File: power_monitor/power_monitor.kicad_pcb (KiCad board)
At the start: 2 copper layers, 60 x 62 mm, 22 parts, among them J1 230V AC Input, J2 230V AC Output, J3 RFID, J4 OLED, J5 WS2812, K1 G2RL-2A-DC5, Q1 FDN339AN, U1 Wemos-D1-mini, U2 ACS723xMATR-10AB

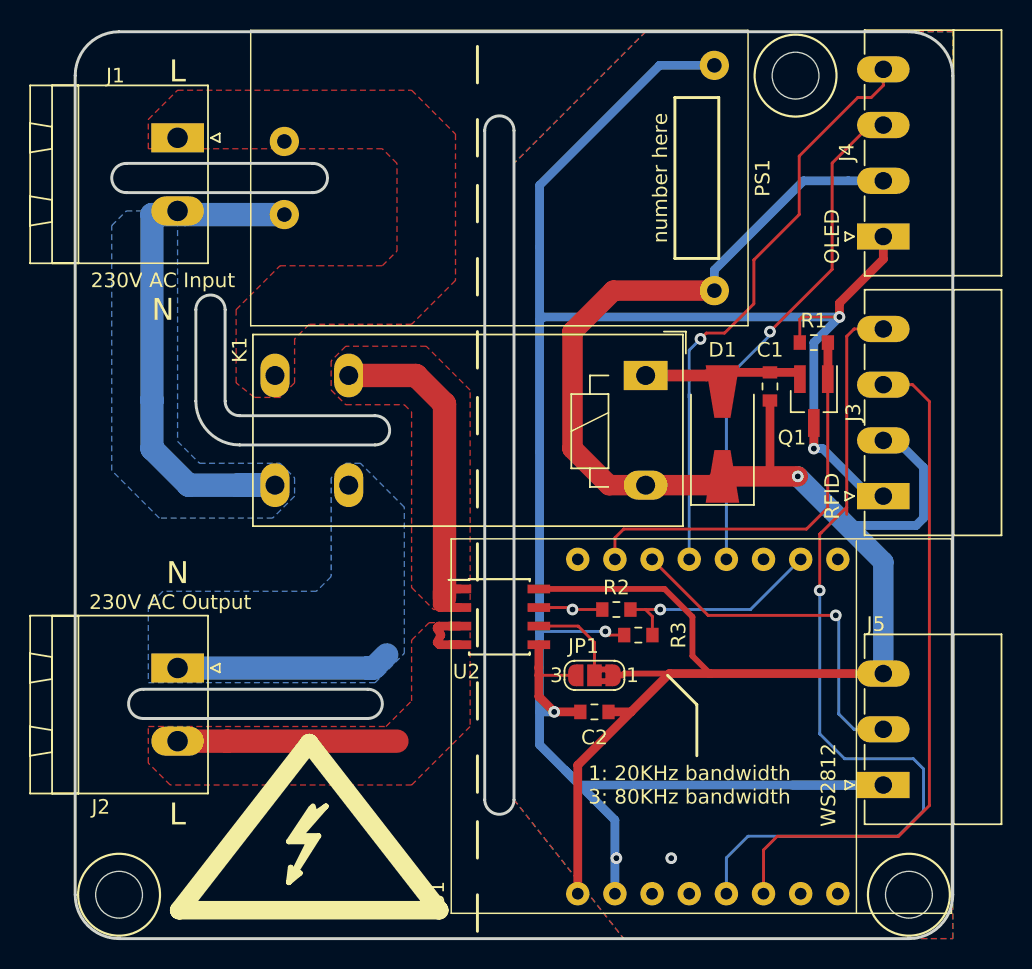
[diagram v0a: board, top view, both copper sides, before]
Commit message: changed diode footprint
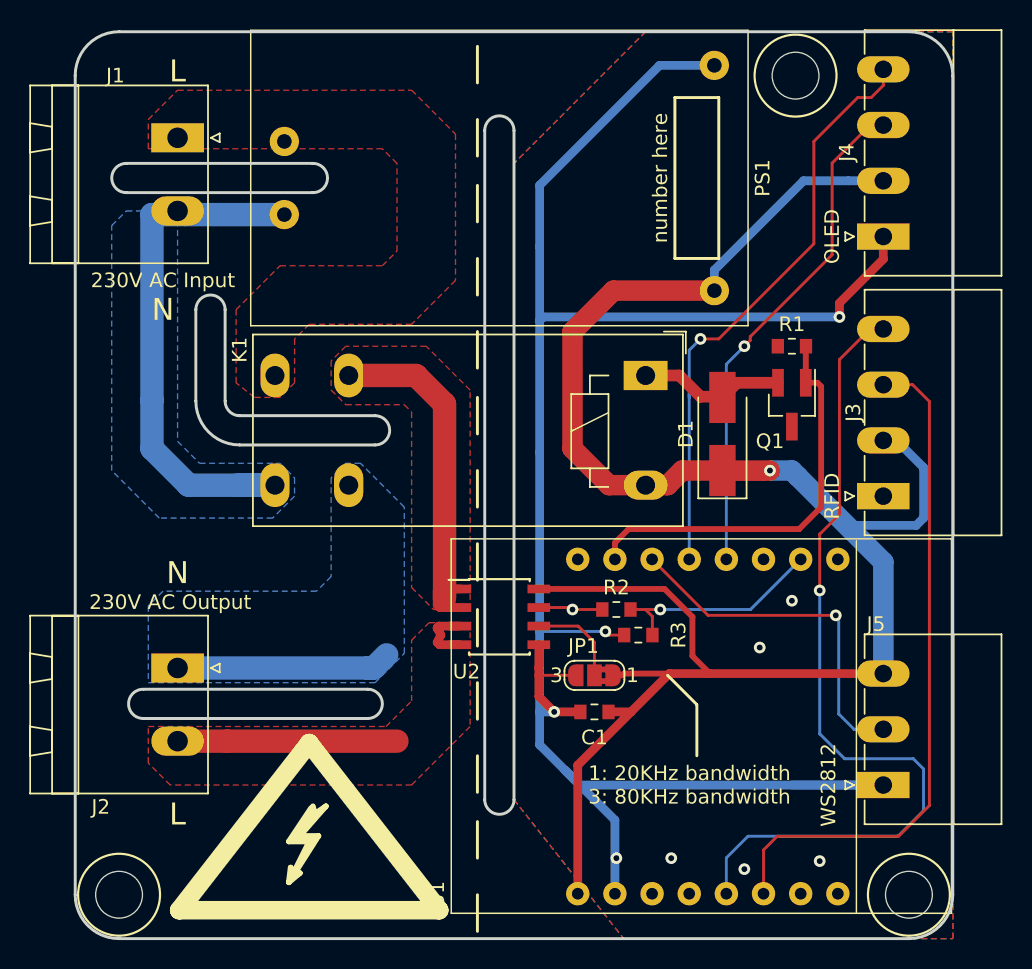
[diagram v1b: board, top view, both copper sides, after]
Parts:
- removed the C1 at (89.5, 60.2)
- D1: footprint Diode_SMD:D_SMA-SMB_Universal_Handsoldering -> Diode_SMD:D_SMA_Handsoldering
- moved Q1 1.52 mm to (91.0, 61.5)
- moved R1 1.52 mm to (91.0, 57.5)
- renumbered C2 to C1
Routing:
- net GND: track 161.4 -> 139.5 mm, vias 6 -> 9
- net +5V: track 150.2 -> 143.5 mm
- net SDA: track 59.4 -> 58.2 mm
- net Net-(D1-Pad2): track 10.7 -> 10.1 mm

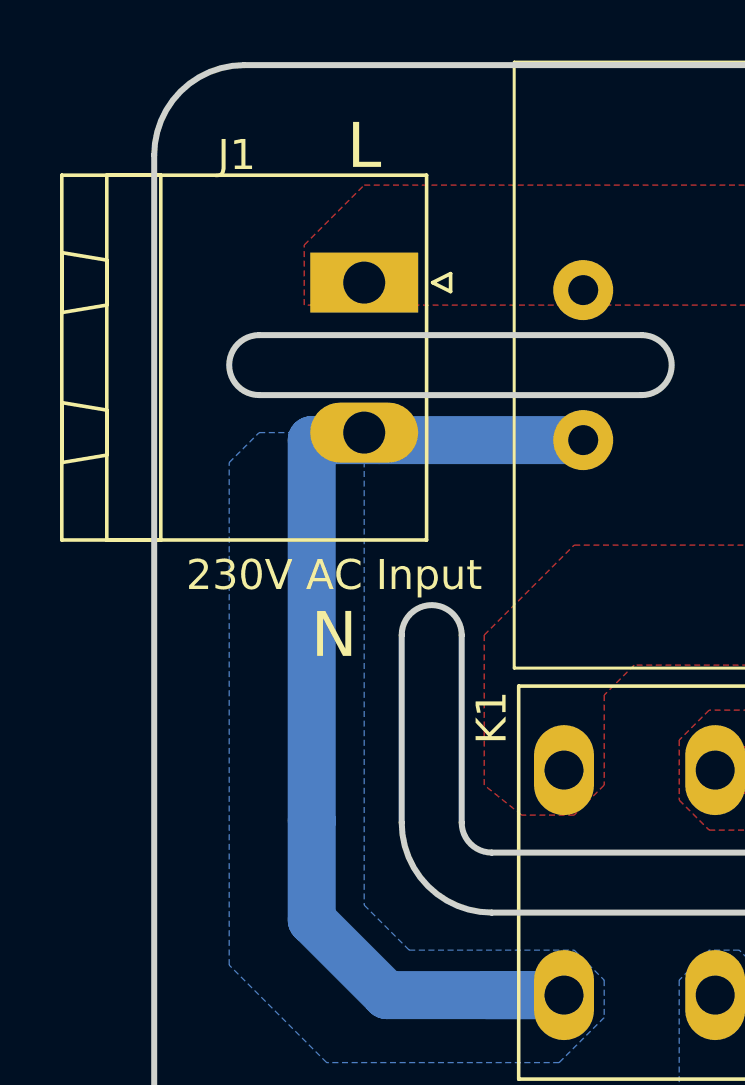
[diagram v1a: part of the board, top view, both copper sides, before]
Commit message: Moved live in connector a bit
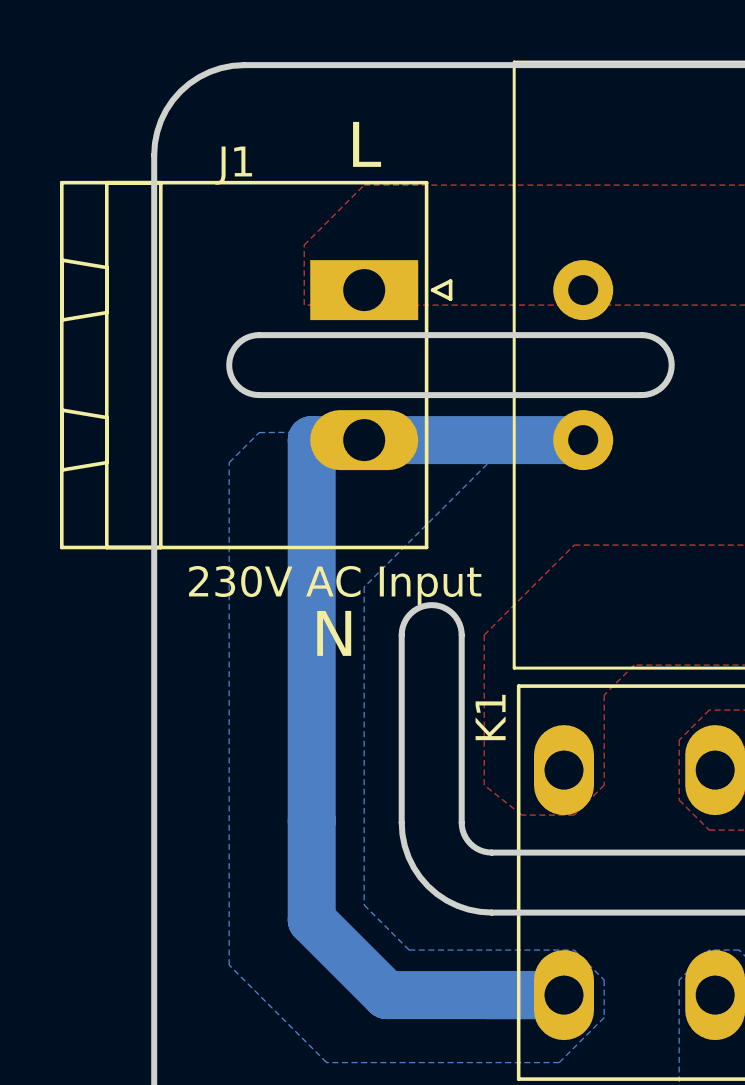
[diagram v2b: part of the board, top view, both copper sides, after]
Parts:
- moved J1 0.25 mm to (49.0, 43.5)
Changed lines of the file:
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@@
-(kicad_pcb (version 20171130) (host pcbnew "(5.0.0-rc2-dev-158-g52ab6216c)")
+(kicad_pcb (version 20171130) (host pcbnew 5.0-dev-unknown-9241a39~61~ubuntu17.10.1)
   (general
     (thickness 1.6)
@@
   )
   (module Connector_Phoenix_MSTB:PhoenixContact_MSTBA_2,5_2-G_1x02_P5.00mm_Horizontal (layer F.Cu)
-    (at 49 43.25 270)
+    (at 49 43.5 270)
     (descr "Generic Phoenix Contact connector footprint for: MSTBA_2,5/2-G; number of pins: 02; pin pitch: 5.00mm; Angled || order number: 1757475 12A || order number: 1923759 16A (HC)")
     (tags "phoenix_contact connector MSTBA_01x02_G_5.00mm")
@@
       (pts
         (xy 50.5 65.5) (xy 56 65.5) (xy 57 66.5) (xy 57 67.75) (xy 55.5 69.25)
-        (xy 47.75 69.25) (xy 44.5 66) (xy 44.5 49.25) (xy 45.5 48.25) (xy 49 48.25)
-        (xy 49 64)
+        (xy 47.75 69.25) (xy 44.5 66) (xy 44.5 49.25) (xy 45.5 48.25) (xy 53.1 48.2)
+        (xy 53.1 49.3) (xy 49 53.4) (xy 49 64)
       )
     )
